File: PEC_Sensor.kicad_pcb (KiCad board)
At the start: 2 copper layers, 3 parts, among them IC1 TC4420EOA, U3 ESP-12F

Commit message: revision 2 finished
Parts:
- added D1: SS34, Diode_SMD:D_SMA, F.Cu at (108.5, 73.5)
- added J1: Conn_01x03_Pin, Connector_JST:JST_EH_S3B-EH_1x03_P2.50mm_Horizontal, F.Cu at (95.1, 57.8)
- added J2: Conn_01x03_Pin, Connector_JST:JST_EH_S3B-EH_1x03_P2.50mm_Horizontal, F.Cu at (95.1, 68.1)
- added U2: OPA820, Package_TO_SOT_SMD:SOT-353_SC-70-5, F.Cu at (104.0, 80.0)
- IC1: value TC4420EOA -> TC4420
- U3: value ESP-12F -> TPS54331; footprint RF_Module:ESP-12E -> Package_SO:HVSSOP-10-1EP_3x3mm_P0.5mm_EP1.57x1.88mm_ThermalVias
- moved U3 110.3 mm to (96.1, 80.0)
- moved A1 21.7 mm to (74.3, 54.6)
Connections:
- A1 pad 20: unconnected-(A1-A1-Pad20) -> V_sense
- A1 pad 30: unconnected-(A1-VIN-Pad30) -> +5V
- A1 pad 5: unconnected-(A1-D2-Pad5) -> Pulse
- A1 pad 6: unconnected-(A1-D3-Pad6) -> EnA
- A1 pad 7: unconnected-(A1-D4-Pad7) -> EnB
- IC1 pad 1: unconnected-(IC1-VDD_1-Pad1) -> +12V
- IC1 pad 2: Net-(IC1-INPUT) -> Pulse
- IC1 pad 5: unconnected-(IC1-GND_2-Pad5) -> GND
- IC1 pad 6: unconnected-(IC1-OUTPUT_1-Pad6) -> Net-(IC1-OUTPUT_1)
- U3 pad 1: unconnected-(U3-~{RST}-Pad1) -> Net-(U3-BOOT)
- U3 pad 10: unconnected-(U3-MISO-Pad10) -> (no net)
- U3 pad 11: unconnected-(U3-GPIO9-Pad11) -> (no net)
- U3 pad 2: Net-(U2A--) -> +12V
- U3 pad 3: unconnected-(U3-EN-Pad3) -> Net-(D2-K)
- U3 pad 4: unconnected-(U3-GPIO16-Pad4) -> GND
- U3 pad 5: Net-(IC1-INPUT) -> Net-(U3-VSENSE)
- U3 pad 6: unconnected-(U3-GPIO12-Pad6) -> Net-(U3-COMP)
- U3 pad 7: unconnected-(U3-GPIO13-Pad7) -> Net-(U3-EN)
- U3 pad 8: unconnected-(U3-VCC-Pad8) -> Net-(U3-SS)
- U3 pad 9: unconnected-(U3-CS0-Pad9) -> GND

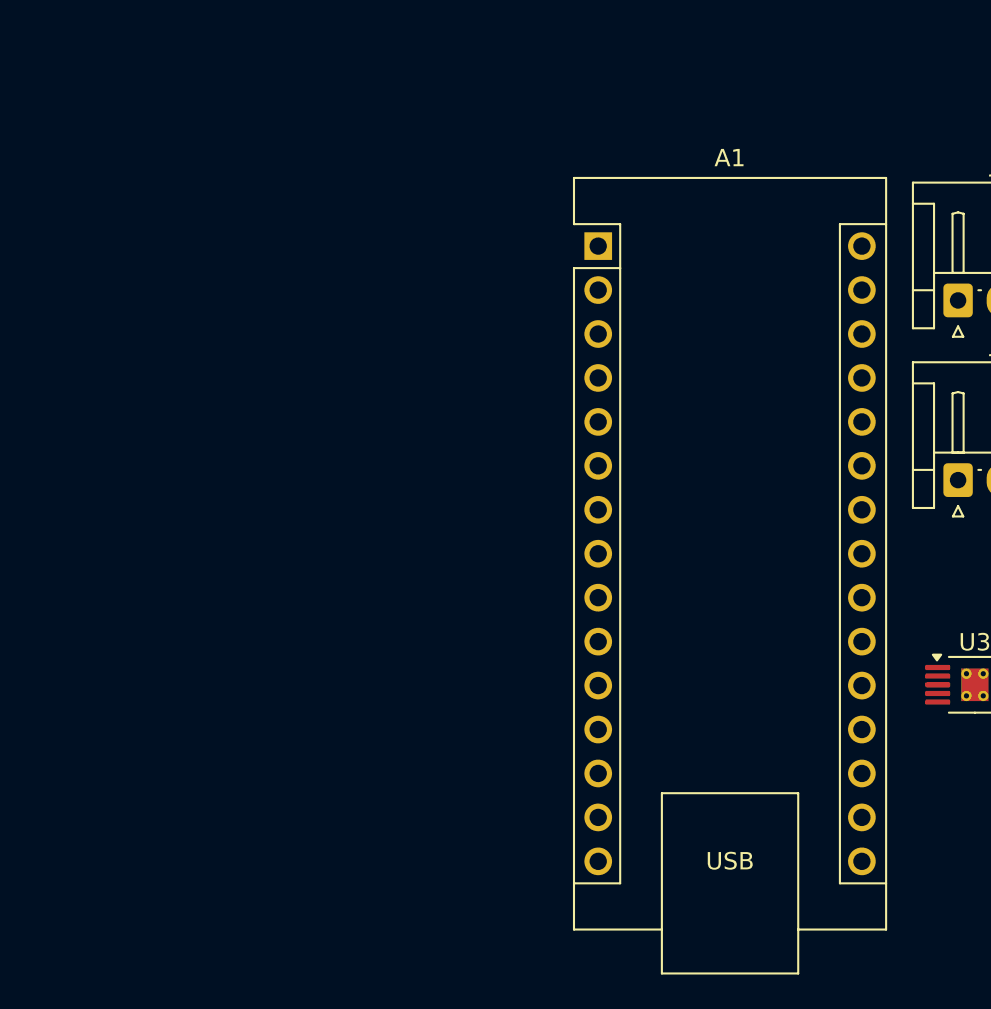
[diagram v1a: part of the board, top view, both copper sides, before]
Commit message: fixed gitignore
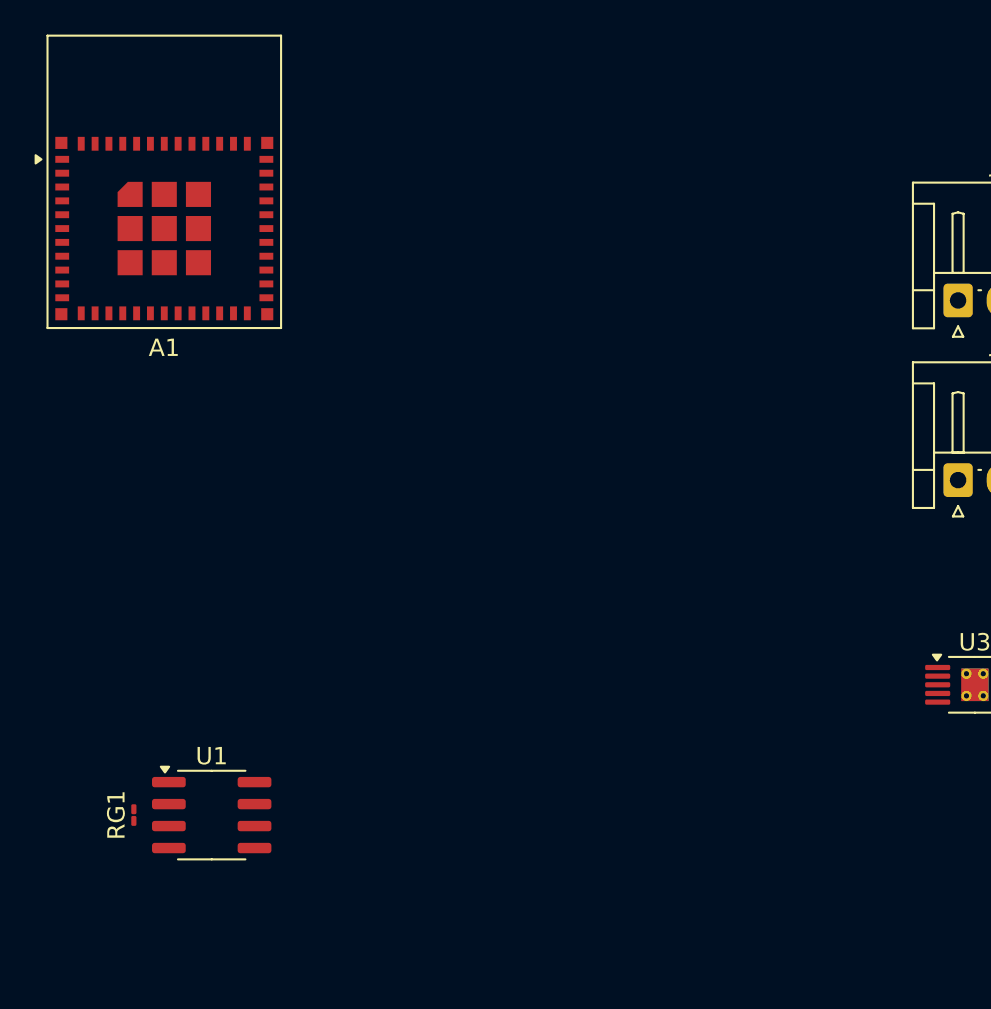
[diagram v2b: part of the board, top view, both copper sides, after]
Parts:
- added RG1: 162 Ω, Resistor_SMD:R_01005_0402Metric_Pad0.57x0.30mm_HandSolder, F.Cu at (47.5, 87.5)
- added U1: AD8221, Package_SO:SOIC-8_3.9x4.9mm_P1.27mm, F.Cu at (52.0, 87.5)
- A1: footprint Module:Arduino_Nano -> RF_Module:ESP32-C6-MINI-1
- D1: value SS34 -> CDBA340L-HF
- moved A1 25.1 mm to (49.3, 53.6)

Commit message: jan 29
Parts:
- removed A1: Arduino_Nano_ESP32, RF_Module:ESP32-C6-MINI-1
- removed D1: CDBA340L-HF, Diode_SMD:D_SMA
- removed IC1: TC4420, Package_SO:SOIC-8_3.9x4.9mm_P1.27mm
- removed J1: Conn_01x03_Pin, Connector_JST:JST_EH_S3B-EH_1x03_P2.50mm_Horizontal
- added C10: 1.0uF, Capacitor_SMD:C_0603_1608Metric, F.Cu at (104.5, 94.5)
- added C11: 0.1uF, Capacitor_SMD:C_0603_1608Metric, F.Cu at (101.2, 75.2)
- added C12: 0.1uF, Capacitor_SMD:C_0603_1608Metric, F.Cu at (97.5, 77.9)
- added C13: 10uF, Capacitor_SMD:C_0603_1608Metric, F.Cu at (107.7, 74.2)
- added C14: 0.1uF, Capacitor_SMD:C_0603_1608Metric, F.Cu at (106.4, 69.0)
- added C15: 0.1uF, Capacitor_SMD:C_0603_1608Metric, F.Cu at (102.5, 77.9)
- added J3: Conn_01x15_Pin, Connector_PinHeader_2.54mm:PinHeader_1x15_P2.54mm_Vertical, F.Cu at (125.5, 82.4)
- added J6: Conn_01x02_Pin, Connector_JST:JST_EH_S2B-EH_1x02_P2.50mm_Horizontal, F.Cu at (89.5, 71.5)
- added J7: Conn_01x02_Pin, Connector_BarrelJack:BarrelJack_Horizontal, F.Cu at (87.5, 106.0)
- added J9: Conn_01x02_Pin, Connector_JST:JST_EH_S2B-EH_1x02_P2.50mm_Horizontal, F.Cu at (107.0, 112.5)
- added L1: 3.3uH, Inductor_SMD:L_Taiyo-Yuden_NR-50xx, F.Cu at (90.0, 94.0)
- added R7: 10.6kΩ, Resistor_SMD:R_0603_1608Metric, F.Cu at (101.2, 73.7)
- added R8: 10.6kΩ, Resistor_SMD:R_0603_1608Metric, F.Cu at (99.0, 74.4)
- added U4: TC4420, Package_SO:SOIC-8_3.9x4.9mm_P1.27mm, F.Cu at (104.5, 90.0)
- J2: value Conn_01x03_Pin -> Conn_01x15_Pin; footprint Connector_JST:JST_EH_S3B-EH_1x03_P2.50mm_Horizontal -> Connector_PinHeader_2.54mm:PinHeader_1x15_P2.54mm_Vertical
- RG1: value 162 Ω -> 162Ω; footprint Resistor_SMD:R_01005_0402Metric_Pad0.57x0.30mm_HandSolder -> Resistor_SMD:R_0603_1608Metric
- U1: value AD8221 -> AP62301WU; footprint Package_SO:SOIC-8_3.9x4.9mm_P1.27mm -> Package_TO_SOT_SMD:TSOT-23-6
- U2: value OPA820 -> AD8221; footprint Package_TO_SOT_SMD:SOT-353_SC-70-5 -> Package_SO:SOIC-8_3.9x4.9mm_P1.27mm
- U3: value TPS54331 -> OPA820; footprint Package_SO:HVSSOP-10-1EP_3x3mm_P0.5mm_EP1.57x1.88mm_ThermalVias -> Package_TO_SOT_SMD:SOT-23-5
- moved RG1 52.9 mm to (97.5, 70.2)
- moved U1 38.8 mm to (88.5, 100.6)
- moved J2 14.8 mm to (99.0, 82.4)
- moved U2 10.0 mm to (102.0, 70.2)
- moved U3 4.34 mm to (100.0, 78.0), turned to -90 degrees
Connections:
- net Net-(J2-Pin_3) renamed VOUT_USB
- J2 pad 1: Net-(J2-Pin_1) -> A0
- U1 pad 1: Net-(J3-Pin_1) -> GND
- U1 pad 2: Net-(RG1-Pad2) -> Net-(U1-SW)
- U1 pad 3: Net-(RG1-Pad1) -> 12V
- U1 pad 5: GND -> unconnected-(U1-EN-Pad5)
- U1 pad 6: GND -> Net-(U1-BST)
- U2 pad 2: GND -> Net-(RG1-Pad2)
- U2 pad 3: V_sense -> Net-(RG1-Pad1)
- U2 pad 4: V_sense -> Net-(J6-Pin_1)
- U2 pad 5: +5V -> GND
- U3 pad 1: Net-(U3-BOOT) -> A0
- U3 pad 2: +12V -> GND
- U3 pad 4: GND -> A0
- U3 pad 5: Net-(U3-VSENSE) -> 5V
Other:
- board outline added: 45 x 60 mm

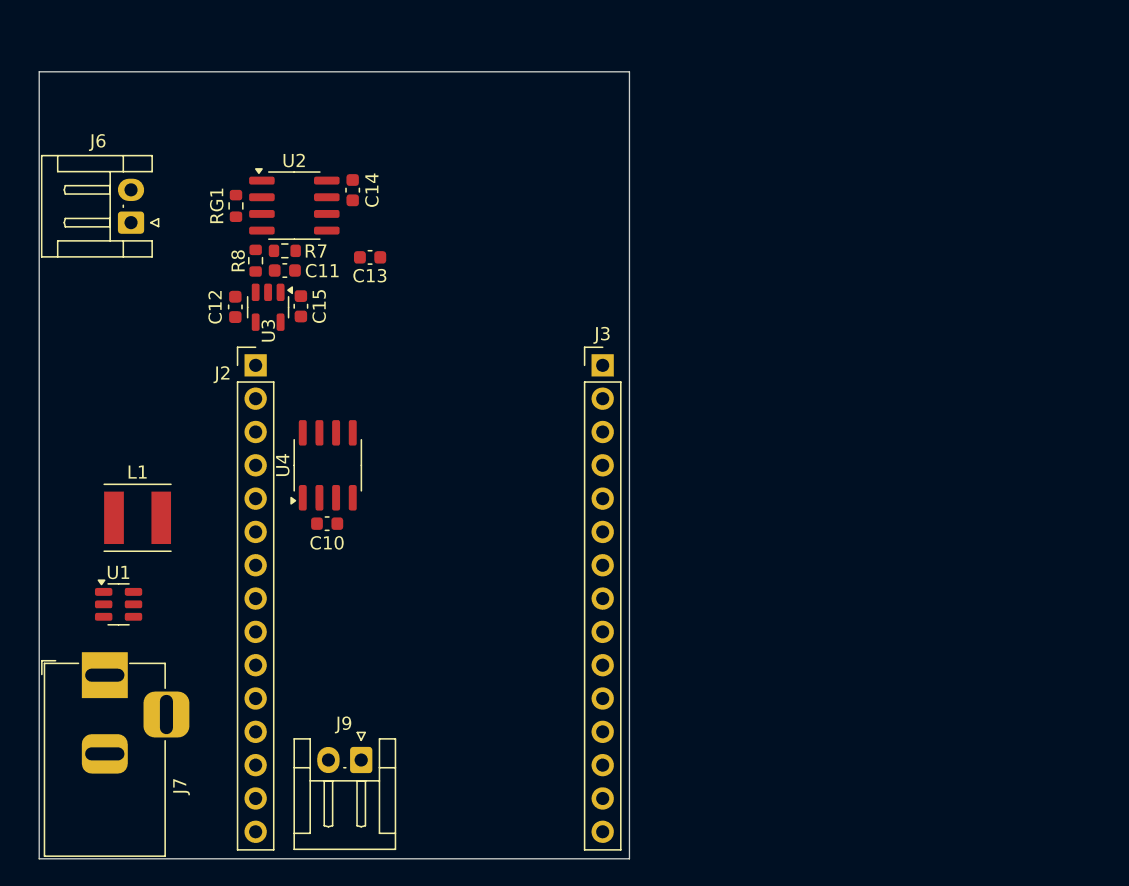
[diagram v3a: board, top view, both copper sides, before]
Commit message: finished footprints
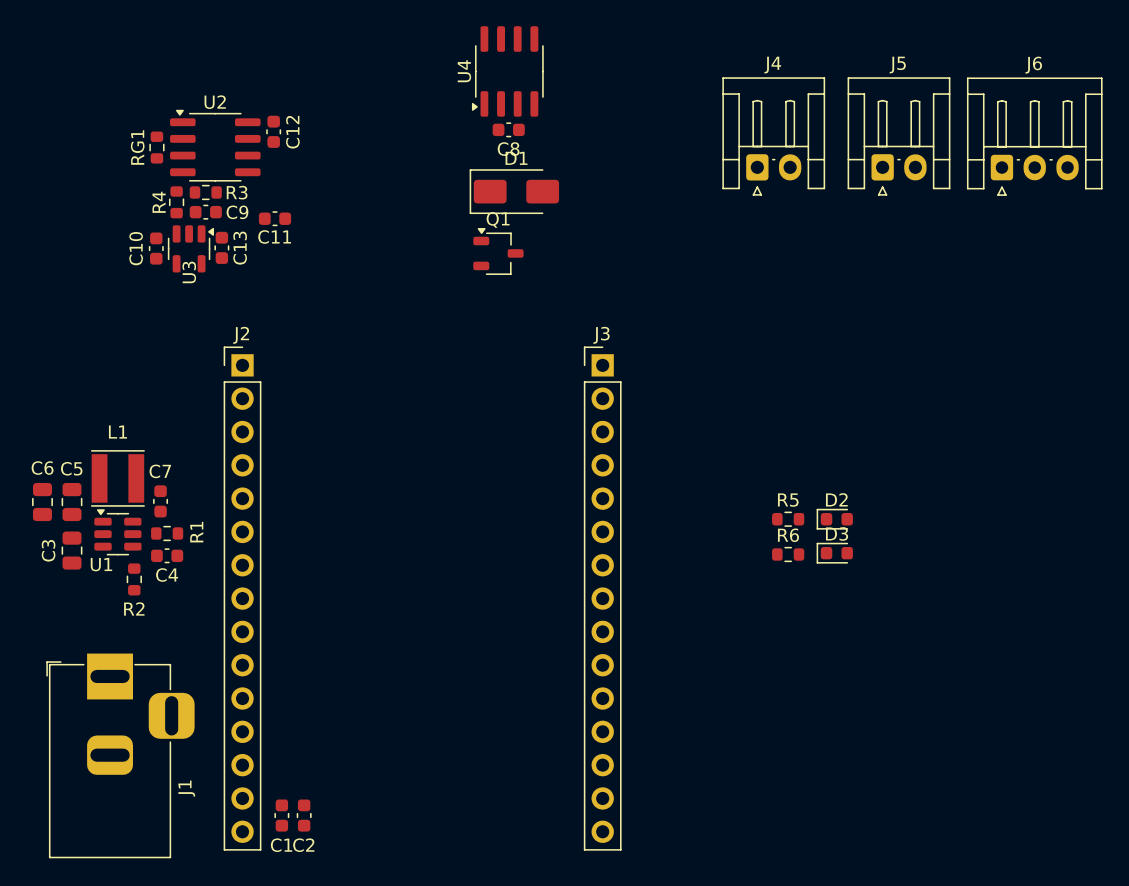
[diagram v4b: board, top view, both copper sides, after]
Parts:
- removed J7: Conn_01x02_Pin, Connector_BarrelJack:BarrelJack_Horizontal
- removed J9: Conn_01x02_Pin, Connector_JST:JST_EH_S2B-EH_1x02_P2.50mm_Horizontal
- added C1: 0.1uF, Capacitor_SMD:C_0603_1608Metric, F.Cu at (101.0, 116.7)
- added C2: 47uF, Capacitor_SMD:C_0603_1608Metric, F.Cu at (102.7, 116.7)
- added C3: 10uF, Capacitor_SMD:C_0805_2012Metric, F.Cu at (85.0, 96.5)
- added C4: 100pF, Capacitor_SMD:C_0603_1608Metric, F.Cu at (92.2, 96.9)
- added C5: 22uF, Capacitor_SMD:C_0805_2012Metric, F.Cu at (85.0, 92.8)
- added C6: 22uF, Capacitor_SMD:C_0805_2012Metric, F.Cu at (82.8, 92.8)
- added C7: 330nF, Capacitor_SMD:C_0603_1608Metric, F.Cu at (91.8, 92.8)
- added D1: CDBA340L-HF, Diode_SMD:D_SMA, F.Cu at (118.9, 69.1)
- added D2: LED, LED_SMD:LED_0603_1608Metric, F.Cu at (143.3, 94.1)
- added D3: LED, LED_SMD:LED_0603_1608Metric, F.Cu at (143.3, 96.7)
- added J1: Conn_01x02_Pin, Connector_BarrelJack:BarrelJack_Horizontal, F.Cu at (87.9, 106.1)
- added J4: Sensor Coil, Connector_JST:JST_EH_S2B-EH_1x02_P2.50mm_Horizontal, F.Cu at (137.2, 67.3)
- added J5: Driver Coil, Connector_JST:JST_EH_S2B-EH_1x02_P2.50mm_Horizontal, F.Cu at (146.8, 67.3)
- added Q1: SSM3K336R, Package_TO_SOT_SMD:TSOT-23, F.Cu at (117.5, 73.8)
- added R1: 52.3kΩ, Resistor_SMD:R_0603_1608Metric, F.Cu at (92.2, 95.2)
- added R2: 10kΩ, Resistor_SMD:R_0603_1608Metric, F.Cu at (89.8, 98.7)
- added R5: 470, Resistor_SMD:R_0603_1608Metric, F.Cu at (139.6, 94.1)
- added R6: 470, Resistor_SMD:R_0603_1608Metric, F.Cu at (139.6, 96.8)
- J6: value Conn_01x02_Pin -> Conn_01x03_Pin; footprint Connector_JST:JST_EH_S2B-EH_1x02_P2.50mm_Horizontal -> Connector_JST:JST_EH_S3B-EH_1x03_P2.50mm_Horizontal
- L1: footprint Inductor_SMD:L_Taiyo-Yuden_NR-50xx -> Inductor_SMD:L_Taiyo-Yuden_NR-40xx
- moved J6 66.5 mm to (155.9, 67.3), turned to 0 degrees
- moved C8 33.1 mm to (118.3, 64.4)
- moved U4 33.1 mm to (118.3, 60.0)
- moved C11 7.83 mm to (100.5, 71.2)
- moved C10 7.49 mm to (91.4, 73.5)
- moved C12 7.49 mm to (100.4, 64.6)
- moved C13 7.49 mm to (96.4, 73.4)
- moved R4 7.49 mm to (93.0, 70.0)
- moved U2 7.49 mm to (95.9, 65.8)
- moved U3 7.49 mm to (93.9, 73.5)
- moved RG1 7.49 mm to (91.5, 65.8)
- moved C9 7.49 mm to (95.2, 70.7)
- moved R3 7.49 mm to (95.2, 69.2)
- moved U1 5.35 mm to (88.5, 95.2)
- moved L1 3.35 mm to (88.5, 91.0), turned to 180 degrees
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- renumbered C12 to C10, C13 to C11, C14 to C12, C15 to C13, C10 to C8, C11 to C9, R7 to R3, R8 to R4
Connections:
- J6 pad 1: Net-(J6-Pin_1) -> D5
- J6 pad 2: Net-(J6-Pin_2) -> 5V
- U2 pad 1: Net-(J6-Pin_2) -> Net-(J4-Pin_2)
- U2 pad 4: Net-(J6-Pin_1) -> Net-(J4-Pin_1)
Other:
- board outline removed

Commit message: final design done
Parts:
- added ?: , , F.Cu at (178.4, 97.7)
- added ?: , , F.Cu at (199.8, 64.0)
- added ?: , , F.Cu at (196.9, 110.3)
- added ?: , , F.Cu at (196.9, 92.6)
- added ?: , , F.Cu at (178.4, 95.1)
- added ?: , , F.Cu at (178.4, 77.3)
- added ?: , , F.Cu at (178.4, 92.6)
- added ?: , , F.Cu at (199.8, 128.0)
- added ?: , , F.Cu at (178.4, 82.4)
- added ?: , , F.Cu at (150.8, 128.0)
- added ?: , , F.Cu at (196.9, 77.3)
- added ?: , , F.Cu at (196.9, 85.0)
- added ?: , , F.Cu at (178.4, 87.5)
- added ?: , , F.Cu at (178.4, 85.0)
- added ?: , , F.Cu at (196.9, 95.1)
- added ?: , , F.Cu at (178.4, 79.9)
- added ?: , , F.Cu at (178.4, 100.2)
- added ?: , , F.Cu at (178.4, 90.0)
- added ?: , , F.Cu at (196.9, 82.4)
- added ?: , , F.Cu at (196.9, 105.3)
- added ?: , , F.Cu at (196.9, 79.9)
- added ?: , , F.Cu at (196.9, 74.8)
- added ?: , , F.Cu at (150.8, 64.0)
- added ?: , , F.Cu at (196.9, 97.7)
- added ?: , , F.Cu at (178.4, 74.8)
- added ?: , , F.Cu at (196.9, 90.0)
- added ?: , , F.Cu at (196.9, 87.5)
- added ?: , , F.Cu at (196.9, 107.8)
- added ?: , , F.Cu at (178.4, 102.7)
- added C14: 6.8uF, Capacitor_SMD:C_0603_1608Metric_Pad1.08x0.95mm_HandSolder, F.Cu at (169.0, 81.3)
- added R10: 100kΩ, Resistor_SMD:R_0603_1608Metric_Pad0.98x0.95mm_HandSolder, F.Cu at (159.7, 65.8)
- added R11: 100kΩ, Resistor_SMD:R_0603_1608Metric_Pad0.98x0.95mm_HandSolder, F.Cu at (159.7, 75.4)
- added R7: 1kΩ, Resistor_SMD:R_0603_1608Metric_Pad0.98x0.95mm_HandSolder, F.Cu at (162.1, 79.0)
- added R8: 1kΩ, Resistor_SMD:R_0603_1608Metric_Pad0.98x0.95mm_HandSolder, F.Cu at (159.7, 68.7)
- added R9: 1kΩ, Resistor_SMD:R_0603_1608Metric_Pad0.98x0.95mm_HandSolder, F.Cu at (159.7, 72.5)
- added RV1: 10kΩ, Potentiometer_SMD:Potentiometer_Bourns_TC33X_Vertical, F.Cu at (166.9, 77.5)
- C1, C10, C11, C12, C13, C4, C7, C8, C9: footprint Capacitor_SMD:C_0603_1608Metric -> Capacitor_SMD:C_0603_1608Metric_Pad1.08x0.95mm_HandSolder
- C2: value 47uF -> 10uF; footprint Capacitor_SMD:C_0603_1608Metric -> Capacitor_SMD:C_0603_1608Metric_Pad1.08x0.95mm_HandSolder
- C3, C5, C6: footprint Capacitor_SMD:C_0805_2012Metric -> Capacitor_SMD:C_0805_2012Metric_Pad1.18x1.45mm_HandSolder
- D1: footprint Diode_SMD:D_SMA -> Diode_SMD:D_SMA_Handsoldering
- D2: value LED -> APT2012LZGCK; footprint LED_SMD:LED_0603_1608Metric -> LED_SMD:LED_0805_2012Metric_Pad1.15x1.40mm_HandSolder
- D3: value LED -> APT2012LVBC/D; footprint LED_SMD:LED_0603_1608Metric -> LED_SMD:LED_0805_2012Metric_Pad1.15x1.40mm_HandSolder
- J6: value Conn_01x03_Pin -> Encoder; footprint Connector_JST:JST_EH_S3B-EH_1x03_P2.50mm_Horizontal -> Connector_JST:JST_EH_S4B-EH_1x04_P2.50mm_Horizontal
- R1, R2, R3, R4: footprint Resistor_SMD:R_0603_1608Metric -> Resistor_SMD:R_0603_1608Metric_Pad0.98x0.95mm_HandSolder
- R5: value 470 -> 1k; footprint Resistor_SMD:R_0603_1608Metric -> Resistor_SMD:R_0603_1608Metric_Pad0.98x0.95mm_HandSolder
- R6: value 470 -> 4.7k; footprint Resistor_SMD:R_0603_1608Metric -> Resistor_SMD:R_0603_1608Metric_Pad0.98x0.95mm_HandSolder
- RG1: value 162Ω -> 10k; footprint Resistor_SMD:R_0603_1608Metric -> Resistor_SMD:R_0603_1608Metric_Pad0.98x0.95mm_HandSolder
- moved U4 80.3 mm to (184.2, 105.9)
- moved Q1 79.5 mm to (186.8, 112.8), turned to -90 degrees
- moved D1 78.0 mm to (179.8, 117.8), turned to 180 degrees
- moved J2 77.1 mm to (174.8, 74.8)
- moved U3 76.2 mm to (169.0, 86.5), turned to 0 degrees
- moved R2 75.4 mm to (164.0, 111.7), turned to 0 degrees
- moved C8 75.4 mm to (180.1, 107.5), turned to 90 degrees
- moved J3 75.3 mm to (200.4, 74.8)
- moved C9 75.3 mm to (167.8, 90.6), turned to -90 degrees
- moved C11 74.1 mm to (174.3, 65.3), turned to -90 degrees
- moved C7 73.5 mm to (164.1, 105.8), turned to 0 degrees
- moved C13 73.3 mm to (169.0, 83.5), turned to 0 degrees
- moved C4 72.9 mm to (164.1, 109.7)
- moved R1 72.9 mm to (164.0, 107.8)
- moved U2 72.1 mm to (167.9, 70.6)
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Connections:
- C10 pad 2: A0 -> D32
- J2 pad 1: A0 -> EN
- J2 pad 10: GND -> D27
- J2 pad 11: 3V3 -> D14
- J2 pad 12: EN -> D12
- J2 pad 13: RESET -> D13
- J2 pad 2: GND -> VP
- J2 pad 3: VOUT_USB -> VN
- J2 pad 4: S3 -> D34
- J2 pad 5: S2 -> D35
- J2 pad 6: S1 -> D32
- J2 pad 7: SC -> D33
- J2 pad 8: S0 -> D25
- J2 pad 9: SK -> D26
- J3 pad 1: D0 -> D23
- J3 pad 10: D7 -> RX2
- J3 pad 11: D8 -> D4
- J3 pad 12: RX -> D2
- J3 pad 13: TX -> D15
- J3 pad 2: D1 -> D22
- J3 pad 3: D2 -> TX0
- J3 pad 4: D3 -> RX0
- J3 pad 5: D5 -> D21
- J3 pad 6: 3V3 -> D19
- J3 pad 7: GND -> D18
- J3 pad 9: D6 -> TX2
- J6 pad 1: D5 -> GND
- J6 pad 2: 5V -> D2
- J6 pad 3: D6 -> D4
- Q1 pad 1: Net-(D1-A) -> Net-(Q1-G)
- Q1 pad 2: Net-(Q1-G) -> GND
- Q1 pad 3: GND -> Net-(D1-A)
- U2 pad 1: Net-(J4-Pin_2) -> Net-(U2--)
- U2 pad 4: Net-(J4-Pin_1) -> Net-(U2-+)
- U2 pad 7: Net-(R3-Pad2) -> Net-(RV1-Pad1)
- U3 pad 1: A0 -> D32
- U3 pad 4: A0 -> D32
- U4 pad 2: S3 -> D13
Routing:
- net 12V: track 0.00 -> 55.6 mm
- net D4: track 0.00 -> 30.7 mm
- net D2: track 0.00 -> 27.3 mm
- net Net-(D1-A): track 0.00 -> 17.5 mm
- net D32: track 0.00 -> 17.1 mm
- net Net-(U1-SW): track 0.00 -> 11.7 mm
- net D13: track 0.00 -> 10.7 mm
- net Net-(Q1-G): track 0.00 -> 9.27 mm
- net Net-(U3-+): track 0.00 -> 7.78 mm
- net Net-(U2--): track 0.00 -> 7.73 mm
- net Net-(U2-+): track 0.00 -> 7.73 mm
- net Net-(RV1-Pad1): track 0.00 -> 7.46 mm
- net 5V: track 0.00 -> 6.34 mm, vias 0 -> 12
- net Net-(R3-Pad2): track 0.00 -> 6.09 mm
- net Net-(C10-Pad1): track 0.00 -> 4.55 mm
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- added copper zone on F.Cu, net 12V
- added copper zone on F.Cu, net 5V
- added copper zone on In2.Cu, net 5V
- added copper zone on B.Cu, net GND
- added copper zone on F.Cu, net GND
- added copper zone on In1.Cu, net GND
- added copper zone on F.Cu, net Net-(U1-BST)
- added copper zone on F.Cu, net Net-(U1-FB)
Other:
- board outline added: 55 x 70 mm
- copper layers 2 -> 4
- board text added: "3V3"
- board text added: "5V"
- board text added: "Battery"
- board text added: "D12"
- board text added: "D13"
- board text added: "D14"
- board text added: "D15"
- board text added: "D18"
- board text added: "D19"
- board text added: "D2"
- board text added: "D21"
- board text added: "D22"
- board text added: "D23"
- board text added: "D25"
- board text added: "D26"
- board text added: "D27"
- board text added: "D32"
- board text added: "D33"
- board text added: "D34"
- board text added: "D35"
- board text added: "D4"
- board text added: "D5"
- board text added: "Driver Coil"
- board text added: "EN"
- board text added: "EnA"
- board text added: "EnB"
- board text added: "GND"
- board text added: "Pulsed Eddy Current Sensor V2.0"
- board text added: "RX0"
- board text added: "RX2"
- board text added: "Sensor Coil"
- board text added: "TX0"
- board text added: "TX2"
- board text added: "VIN"
- board text added: "VN"
- board text added: "VP"
- board text added: "WAFFLE Systems MECH X TRON 2026"
